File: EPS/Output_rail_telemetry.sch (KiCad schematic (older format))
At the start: 12 parts

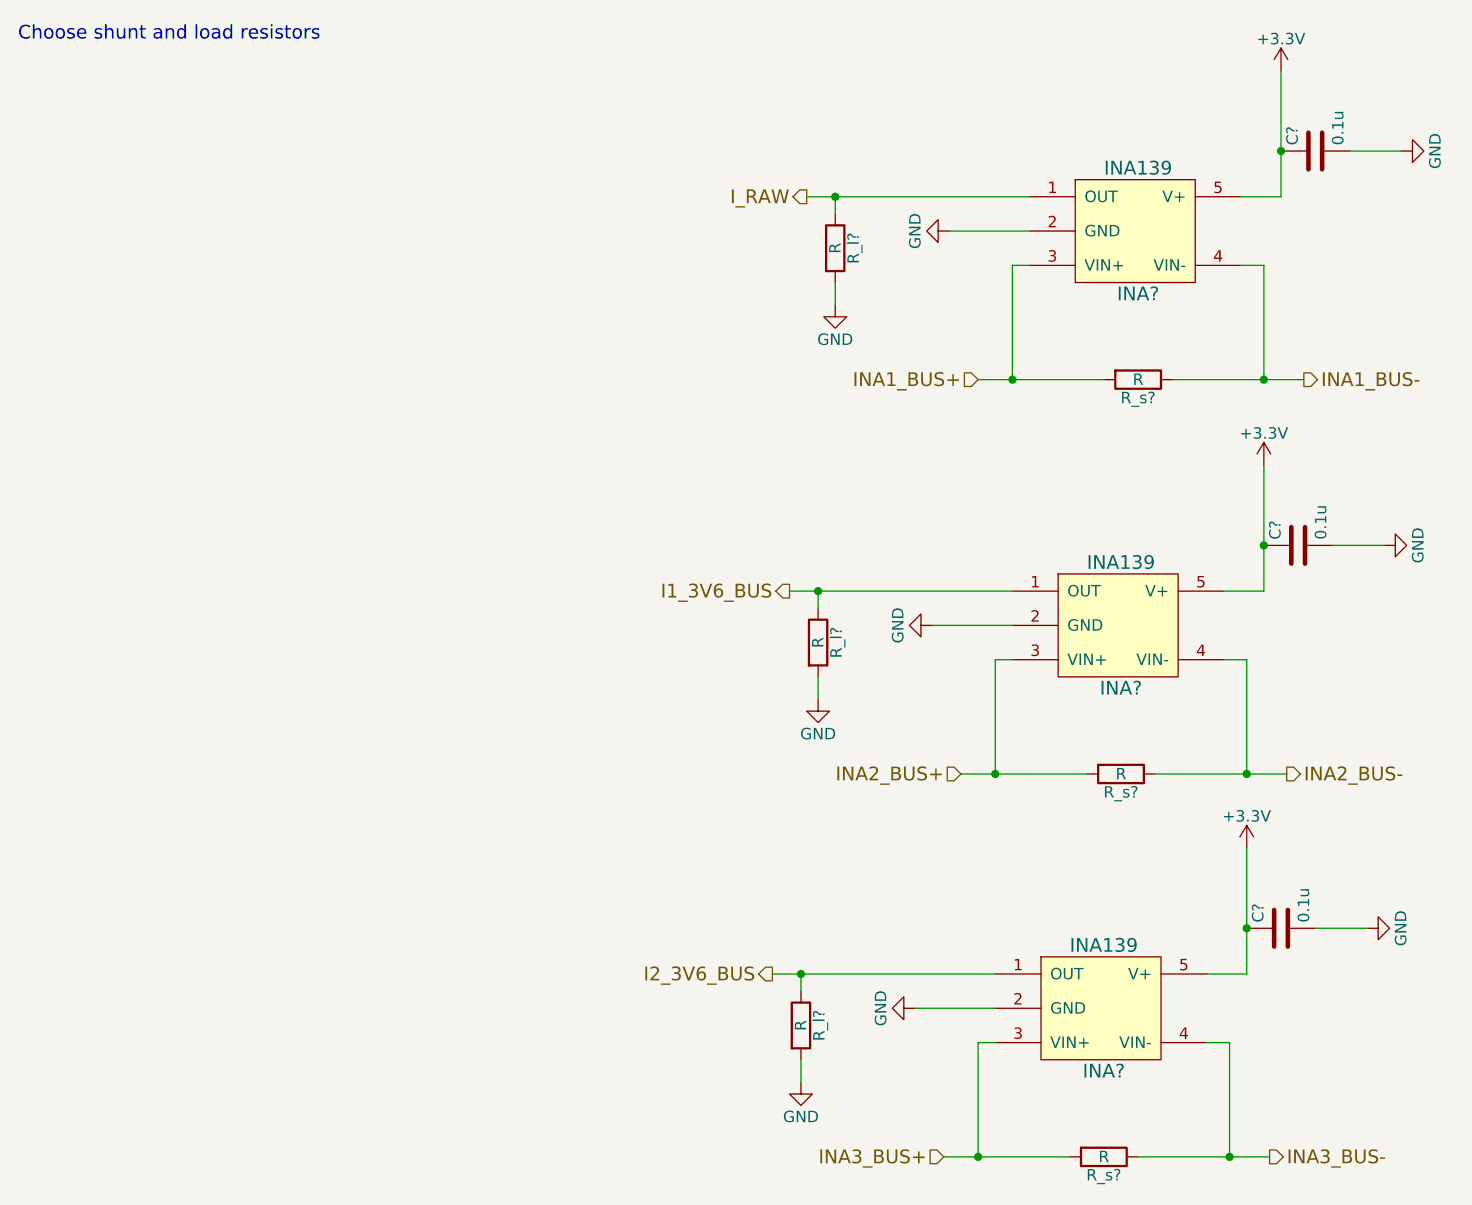
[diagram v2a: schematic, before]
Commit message: Finalized SCH (beta version) and started pcb
Capacitor banks might need to be reassigned to other locations.
No RBF pin on this SCH or PCB.
Battery gound deployment switch is fully mechanical (no mosfet switch on low side).
PCB of the prototype started. Main power converters and current measuring devices layed out.
SCH still requires ESD protection diodes!
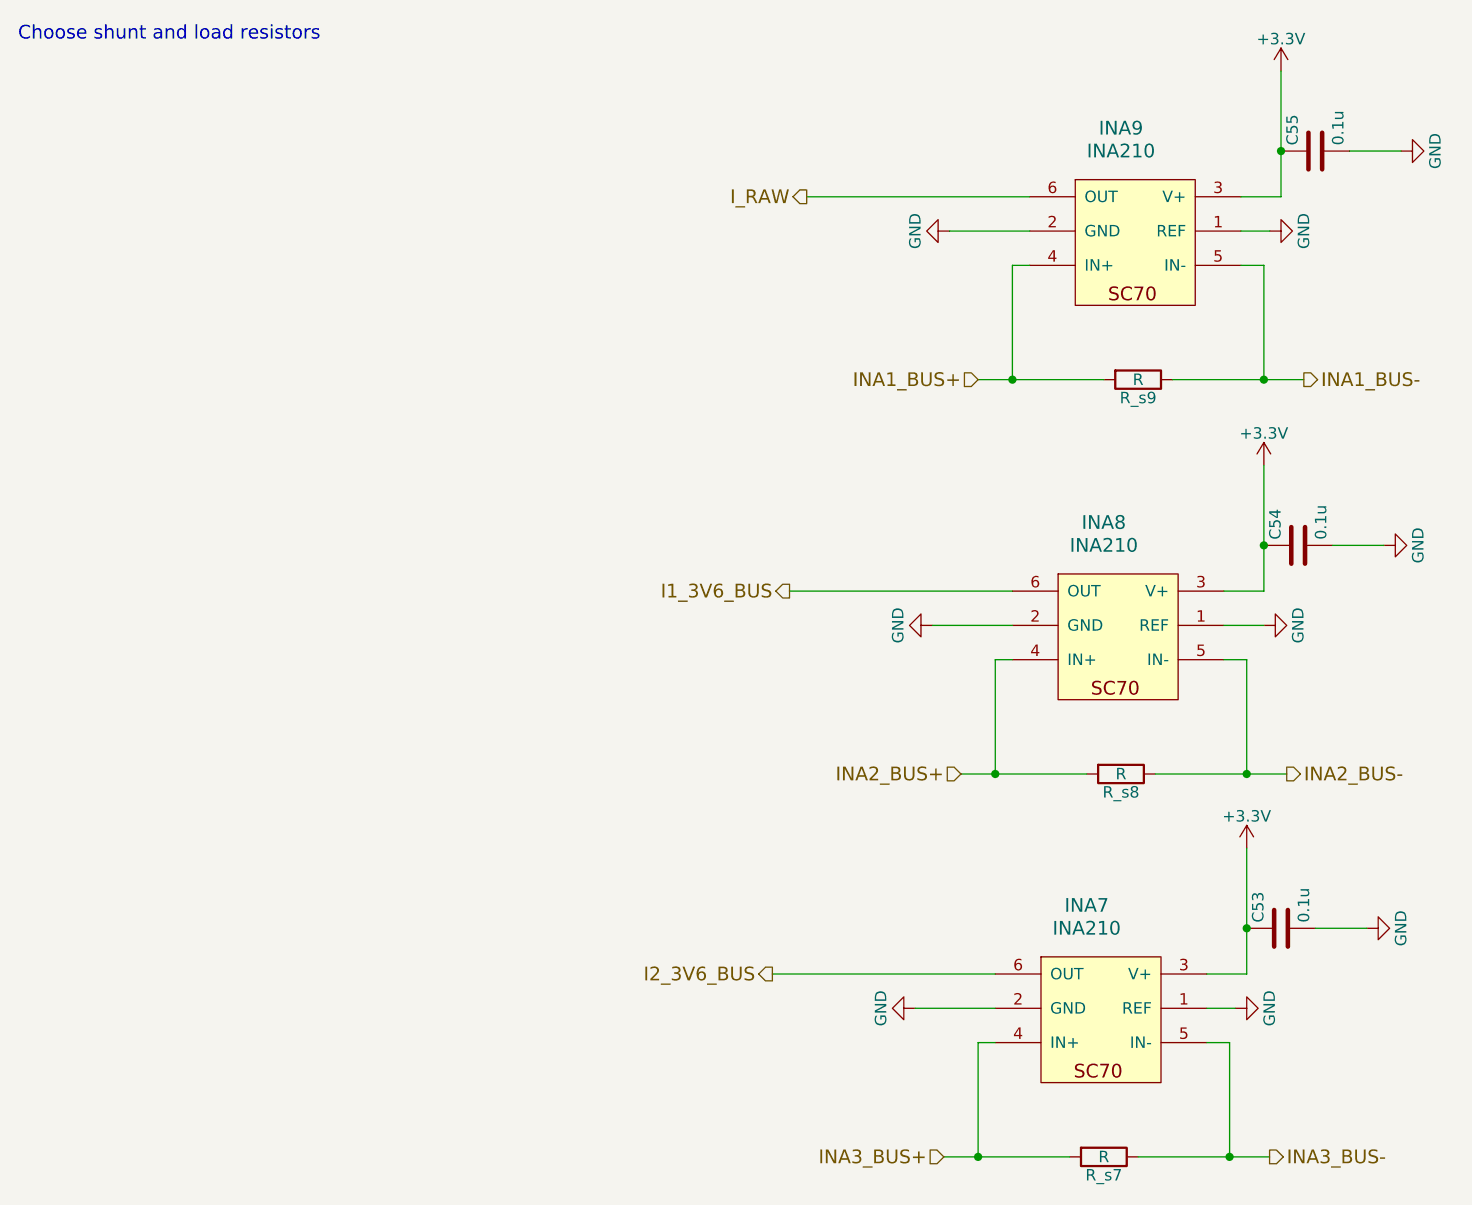
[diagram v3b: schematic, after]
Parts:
- removed INA? (x3): INA139, symbol INA139
- removed R_l? (x3): R, symbol R
- added INA7, INA8, INA9: INA210, TO_SOT_Packages_SMD:SOT-363_SC-70-6, symbol INA210
- C53, C54, C55: renamed from C?; footprint (none) -> Capacitors_SMD:C_0603
- R_s7, R_s8, R_s9: renamed from R_s?; footprint (none) -> Resistors_SMD:R_0805
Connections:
- net +3V3: now also INA7.3 (V+), INA8.3 (V+), INA9.3 (V+)
- net GND: now also INA7.1 (REF), INA7.2 (GND), INA8.1 (REF), INA8.2 (GND), INA9.1 (REF), INA9.2 (GND)
- net I1_3V6_BUS: now also INA8.6 (OUT)
- net I2_3V6_BUS: now also INA7.6 (OUT)
- net INA1_BUS+: now also INA9.4 (IN+)
- net INA1_BUS-: now also INA9.5 (IN-)
- net INA2_BUS+: now also INA8.4 (IN+)
- net INA2_BUS-: now also INA8.5 (IN-)
- net INA3_BUS+: now also INA7.4 (IN+)
- net INA3_BUS-: now also INA7.5 (IN-)
- net I_RAW: now also INA9.6 (OUT)
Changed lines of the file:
@@
 $Descr A4 11693 8268
 encoding utf-8
-Sheet 12 14
+Sheet 11 14
 Title "Output rail telemetry"
-Date "2018-02-15"
+Date "2018-02-22"
 Rev "R1"
 Comp ""
@@
 $EndDescr
 $Comp
-L INA139 INA?
-U 1 1 5A9B6730
-P 5625 1550
-F 0 "INA?" H 5625 1275 60  0000 C CNN
-F 1 "INA139" H 5625 1825 60  0000 C CNN
-F 2 "" H 5500 1600 60  0001 C CNN
-F 3 "" H 5500 1600 60  0001 C CNN
-	1    5625 1550
-	1    0    0    -1
-$EndComp
-$Comp
-L R R_s?
+L R R_s9
 U 1 1 5A9B6737
 P 5625 2200
-F 0 "R_s?" V 5705 2200 50  0000 C CNN
+F 0 "R_s9" V 5705 2200 50  0000 C CNN
 F 1 "R" V 5625 2200 50  0000 C CNN
-F 2 "" V 5555 2200 50  0001 C CNN
+F 2 "Resistors_SMD:R_0805" V 5555 2200 50  0001 C CNN
 F 3 "" H 5625 2200 50  0001 C CNN
 	1    5625 2200
@@
 $EndComp
 $Comp
-L R R_l?
-U 1 1 5A9B673E
-P 4300 1625
-F 0 "R_l?" V 4380 1625 50  0000 C CNN
-F 1 "R" V 4300 1625 50  0000 C CNN
-F 2 "" V 4230 1625 50  0001 C CNN
-F 3 "" H 4300 1625 50  0001 C CNN
-	1    4300 1625
-	1    0    0    -1
-$EndComp
-$Comp
-L C C?
+L C C55
 U 1 1 5A9B6745
 P 6400 1200
-F 0 "C?" H 6425 1300 50  0000 L CNN
+F 0 "C55" H 6425 1300 50  0000 L CNN
 F 1 "0.1u" H 6425 1100 50  0000 L CNN
-F 2 "" H 6438 1050 50  0001 C CNN
+F 2 "Capacitors_SMD:C_0603" H 6438 1050 50  0001 C CNN
 F 3 "" H 6400 1200 50  0001 C CNN
 	1    6400 1200
@@
 $EndComp
 $Comp
-L GND #PWR?
+L GND #PWR0123
 U 1 1 5A9B674C
 P 4800 1550
-F 0 "#PWR?" H 4800 1300 50  0001 C CNN
+F 0 "#PWR0123" H 4800 1300 50  0001 C CNN
 F 1 "GND" H 4800 1400 50  0000 C CNN
 F 2 "" H 4800 1550 50  0001 C CNN
@@
 $EndComp
 $Comp
-L +3.3V #PWR?
+L +3.3V #PWR0124
 U 1 1 5A9B6752
 P 6250 850
-F 0 "#PWR?" H 6250 700 50  0001 C CNN
+F 0 "#PWR0124" H 6250 700 50  0001 C CNN
 F 1 "+3.3V" H 6250 990 50  0000 C CNN
 F 2 "" H 6250 850 50  0001 C CNN
@@
 Connection ~ 6250 1200
 $Comp
-L GND #PWR?
+L GND #PWR0125
 U 1 1 5A9B675B
 P 6775 1200
-F 0 "#PWR?" H 6775 950 50  0001 C CNN
+F 0 "#PWR0125" H 6775 950 50  0001 C CNN
 F 1 "GND" H 6775 1050 50  0000 C CNN
 F 2 "" H 6775 1200 50  0001 C CNN
@@
 Wire Wire Line
 	6175 1700 6075 1700
-$Comp
-L GND #PWR?
-U 1 1 5A9B6769
-P 4300 1875
-F 0 "#PWR?" H 4300 1625 50  0001 C CNN
-F 1 "GND" H 4300 1725 50  0000 C CNN
-F 2 "" H 4300 1875 50  0001 C CNN
-F 3 "" H 4300 1875 50  0001 C CNN
-	1    4300 1875
-	1    0    0    -1
-$EndComp
-Wire Wire Line
-	4300 1875 4300 1775
 Wire Wire Line
 	4175 1400 5150 1400
-Wire Wire Line
-	4300 1400 4300 1475
 Text HLabel 4175 1400 0    60   Output ~ 0
 I_RAW
-Connection ~ 4300 1400
 Text HLabel 4925 2200 0    60   Input ~ 0
 INA1_BUS+
@@
 Connection ~ 6175 2200
 $Comp
-L INA139 INA?
-U 1 1 5A9B6778
-P 5550 3275
-F 0 "INA?" H 5550 3000 60  0000 C CNN
-F 1 "INA139" H 5550 3550 60  0000 C CNN
-F 2 "" H 5425 3325 60  0001 C CNN
-F 3 "" H 5425 3325 60  0001 C CNN
-	1    5550 3275
-	1    0    0    -1
-$EndComp
-$Comp
-L R R_s?
+L R R_s8
 U 1 1 5A9B677F
 P 5550 3925
-F 0 "R_s?" V 5630 3925 50  0000 C CNN
+F 0 "R_s8" V 5630 3925 50  0000 C CNN
 F 1 "R" V 5550 3925 50  0000 C CNN
-F 2 "" V 5480 3925 50  0001 C CNN
+F 2 "Resistors_SMD:R_0805" V 5480 3925 50  0001 C CNN
 F 3 "" H 5550 3925 50  0001 C CNN
 	1    5550 3925
@@
 $EndComp
 $Comp
-L R R_l?
-U 1 1 5A9B6786
-P 4225 3350
-F 0 "R_l?" V 4305 3350 50  0000 C CNN
-F 1 "R" V 4225 3350 50  0000 C CNN
-F 2 "" V 4155 3350 50  0001 C CNN
-F 3 "" H 4225 3350 50  0001 C CNN
-	1    4225 3350
-	1    0    0    -1
-$EndComp
-$Comp
-L C C?
+L C C54
 U 1 1 5A9B678D
 P 6325 2925
-F 0 "C?" H 6350 3025 50  0000 L CNN
+F 0 "C54" H 6350 3025 50  0000 L CNN
 F 1 "0.1u" H 6350 2825 50  0000 L CNN
-F 2 "" H 6363 2775 50  0001 C CNN
+F 2 "Capacitors_SMD:C_0603" H 6363 2775 50  0001 C CNN
 F 3 "" H 6325 2925 50  0001 C CNN
 	1    6325 2925
@@
 $EndComp
 $Comp
-L GND #PWR?
+L GND #PWR0126
 U 1 1 5A9B6794
 P 4725 3275
-F 0 "#PWR?" H 4725 3025 50  0001 C CNN
+F 0 "#PWR0126" H 4725 3025 50  0001 C CNN
 F 1 "GND" H 4725 3125 50  0000 C CNN
 F 2 "" H 4725 3275 50  0001 C CNN
@@
 $EndComp
 $Comp
-L +3.3V #PWR?
+L +3.3V #PWR0127
 U 1 1 5A9B679A
 P 6175 2575
-F 0 "#PWR?" H 6175 2425 50  0001 C CNN
+F 0 "#PWR0127" H 6175 2425 50  0001 C CNN
 F 1 "+3.3V" H 6175 2715 50  0000 C CNN
 F 2 "" H 6175 2575 50  0001 C CNN
@@
 Connection ~ 6175 2925
 $Comp
-L GND #PWR?
+L GND #PWR0128
 U 1 1 5A9B67A3
 P 6700 2925
-F 0 "#PWR?" H 6700 2675 50  0001 C CNN
+F 0 "#PWR0128" H 6700 2675 50  0001 C CNN
 F 1 "GND" H 6700 2775 50  0000 C CNN
 F 2 "" H 6700 2925 50  0001 C CNN
@@
 	6100 3425 6000 3425
 $Comp
-L GND #PWR?
+L GND #PWR0129
 U 1 1 5A9B67B1
-P 4225 3600
-F 0 "#PWR?" H 4225 3350 50  0001 C CNN
-F 1 "GND" H 4225 3450 50  0000 C CNN
-F 2 "" H 4225 3600 50  0001 C CNN
-F 3 "" H 4225 3600 50  0001 C CNN
-	1    4225 3600
-	1    0    0    -1
-$EndComp
-Wire Wire Line
-	4225 3600 4225 3500
+P 6175 3275
+F 0 "#PWR0129" H 6175 3025 50  0001 C CNN
+F 1 "GND" H 6175 3125 50  0000 C CNN
+F 2 "" H 6175 3275 50  0001 C CNN
+F 3 "" H 6175 3275 50  0001 C CNN
+	1    6175 3275
+	0    -1   -1   0
+$EndComp
 Wire Wire Line
 	4100 3125 5075 3125
-Wire Wire Line
-	4225 3125 4225 3200
 Text HLabel 4100 3125 0    60   Output ~ 0
 I1_3V6_BUS
-Connection ~ 4225 3125
 Text HLabel 4850 3925 0    60   Input ~ 0
 INA2_BUS+
@@
 Text HLabel 4775 5600 0    60   Input ~ 0
 INA3_BUS+
-Connection ~ 4150 4800
 Text HLabel 4025 4800 0    60   Output ~ 0
 I2_3V6_BUS
 Wire Wire Line
-	4150 4800 4150 4875
-Wire Wire Line
 	4025 4800 5000 4800
-Wire Wire Line
-	4150 5275 4150 5175
-$Comp
-L GND #PWR?
+$Comp
+L GND #PWR0130
 U 1 1 5A9B67F9
-P 4150 5275
-F 0 "#PWR?" H 4150 5025 50  0001 C CNN
-F 1 "GND" H 4150 5125 50  0000 C CNN
-F 2 "" H 4150 5275 50  0001 C CNN
-F 3 "" H 4150 5275 50  0001 C CNN
-	1    4150 5275
-	1    0    0    -1
+P 6050 4950
+F 0 "#PWR0130" H 6050 4700 50  0001 C CNN
+F 1 "GND" H 6050 4800 50  0000 C CNN
+F 2 "" H 6050 4950 50  0001 C CNN
+F 3 "" H 6050 4950 50  0001 C CNN
+	1    6050 4950
+	0    -1   -1   0
 $EndComp
 Wire Wire Line
@@
 	6625 4600 6400 4600
 $Comp
-L GND #PWR?
+L GND #PWR0131
 U 1 1 5A9B67EB
 P 6625 4600
-F 0 "#PWR?" H 6625 4350 50  0001 C CNN
+F 0 "#PWR0131" H 6625 4350 50  0001 C CNN
 F 1 "GND" H 6625 4450 50  0000 C CNN
 F 2 "" H 6625 4600 50  0001 C CNN
@@
 	6100 4800 5925 4800
 $Comp
-L +3.3V #PWR?
+L +3.3V #PWR0132
 U 1 1 5A9B67E2
 P 6100 4250
-F 0 "#PWR?" H 6100 4100 50  0001 C CNN
+F 0 "#PWR0132" H 6100 4100 50  0001 C CNN
 F 1 "+3.3V" H 6100 4390 50  0000 C CNN
 F 2 "" H 6100 4250 50  0001 C CNN
@@
 $EndComp
 $Comp
-L GND #PWR?
+L GND #PWR0133
 U 1 1 5A9B67DC
 P 4650 4950
-F 0 "#PWR?" H 4650 4700 50  0001 C CNN
+F 0 "#PWR0133" H 4650 4700 50  0001 C CNN
 F 1 "GND" H 4650 4800 50  0000 C CNN
 F 2 "" H 4650 4950 50  0001 C CNN
@@
 $EndComp
 $Comp
-L C C?
+L C C53
 U 1 1 5A9B67D5
 P 6250 4600
-F 0 "C?" H 6275 4700 50  0000 L CNN
+F 0 "C53" H 6275 4700 50  0000 L CNN
 F 1 "0.1u" H 6275 4500 50  0000 L CNN
-F 2 "" H 6288 4450 50  0001 C CNN
+F 2 "Capacitors_SMD:C_0603" H 6288 4450 50  0001 C CNN
 F 3 "" H 6250 4600 50  0001 C CNN
 	1    6250 4600
@@
 $EndComp
 $Comp
-L R R_l?
-U 1 1 5A9B67CE
-P 4150 5025
-F 0 "R_l?" V 4230 5025 50  0000 C CNN
-F 1 "R" V 4150 5025 50  0000 C CNN
-F 2 "" V 4080 5025 50  0001 C CNN
-F 3 "" H 4150 5025 50  0001 C CNN
-	1    4150 5025
-	1    0    0    -1
-$EndComp
-$Comp
-L R R_s?
+L R R_s7
 U 1 1 5A9B67C7
 P 5475 5600
-F 0 "R_s?" V 5555 5600 50  0000 C CNN
+F 0 "R_s7" V 5555 5600 50  0000 C CNN
 F 1 "R" V 5475 5600 50  0000 C CNN
-F 2 "" V 5405 5600 50  0001 C CNN
+F 2 "Resistors_SMD:R_0805" V 5405 5600 50  0001 C CNN
 F 3 "" H 5475 5600 50  0001 C CNN
 	1    5475 5600
 	0    1    1    0
 $EndComp
-$Comp
-L INA139 INA?
-U 1 1 5A9B67C0
-P 5475 4950
-F 0 "INA?" H 5475 4675 60  0000 C CNN
-F 1 "INA139" H 5475 5225 60  0000 C CNN
-F 2 "" H 5350 5000 60  0001 C CNN
-F 3 "" H 5350 5000 60  0001 C CNN
-	1    5475 4950
-	1    0    0    -1
-$EndComp
 Text Notes 725  725  0    60   ~ 0
 Choose shunt and load resistors
+$Comp
+L INA210 INA9
+U 1 1 5A8DFA23
+P 5350 1325
+F 0 "INA9" H 5550 1550 60  0000 C CNN
+F 1 "INA210" H 5550 1450 60  0000 C CNN
+F 2 "TO_SOT_Packages_SMD:SOT-363_SC-70-6" H 5550 1450 60  0001 C CNN
+F 3 "" H 5550 1450 60  0001 C CNN
+	1    5350 1325
+	1    0    0    -1
+$EndComp
+$Comp
+L GND #PWR0134
+U 1 1 5A9F6F60
+P 6200 1550
+F 0 "#PWR0134" H 6200 1300 50  0001 C CNN
+F 1 "GND" H 6200 1400 50  0000 C CNN
+F 2 "" H 6200 1550 50  0001 C CNN
+F 3 "" H 6200 1550 50  0001 C CNN
+	1    6200 1550
+	0    -1   -1   0
+$EndComp
+Wire Wire Line
+	6200 1550 6075 1550
+$Comp
+L INA210 INA8
+U 1 1 5A9F79E9
+P 5275 3050
+F 0 "INA8" H 5475 3275 60  0000 C CNN
+F 1 "INA210" H 5475 3175 60  0000 C CNN
+F 2 "TO_SOT_Packages_SMD:SOT-363_SC-70-6" H 5475 3175 60  0001 C CNN
+F 3 "" H 5475 3175 60  0001 C CNN
+	1    5275 3050
+	1    0    0    -1
+$EndComp
+$Comp
+L INA210 INA7
+U 1 1 5A9F7A6F
+P 5200 4725
+F 0 "INA7" H 5400 4950 60  0000 C CNN
+F 1 "INA210" H 5400 4850 60  0000 C CNN
+F 2 "TO_SOT_Packages_SMD:SOT-363_SC-70-6" H 5400 4850 60  0001 C CNN
+F 3 "" H 5400 4850 60  0001 C CNN
+	1    5200 4725
+	1    0    0    -1
+$EndComp
+Wire Wire Line
+	5925 4950 6050 4950
+Wire Wire Line
+	6175 3275 6000 3275
 $EndSCHEMATC
